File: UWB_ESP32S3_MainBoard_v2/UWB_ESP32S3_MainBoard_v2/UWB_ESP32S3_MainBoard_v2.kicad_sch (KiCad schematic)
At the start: 7 parts, among them J1 ESP32_S3_2, J2 ESP32_S3_1, J3 BNO085, J4 DRV8833_L_OUT, J5 DRV8833_L_IN, J6 DRV8833_R_OUT, J7 DRV8833_R_IN

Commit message: PCB재설계
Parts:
- added C1, C3: 470uF_16V, symbol Device:C
- added C10, C2, C4, C6, C8, C9: 0.1uF_50V, symbol Device:C
- added C5: 100uF_16V, symbol Device:C
- added C7: 100uF_50V, symbol Device:C
- added D1: D_Schottky, symbol Device:D_Schottky
- added D2: VBAT_LED, symbol Device:LED
- added D3: 5V0_LED, symbol Device:LED
- added D4: VCC_LED, symbol Device:LED
- added F1: PTC_2A, symbol Device:Fuse
- added J10: MP1584EN_IN, symbol Connector_Generic:Conn_01x06
- added J11: MP1584EN_OUT, symbol Connector_Generic:Conn_01x06
- added J12: MINI360_IN, symbol Connector_Generic:Conn_01x04
- added J13: MINI360_OUT, symbol Connector_Generic:Conn_01x04
- added J14: VBAT, symbol Connector:Screw_Terminal_01x02
- added J8: TAU_1201, symbol Connector_Generic:Conn_01x07
- added J9: ESP32_UWBAOA_UART, symbol Connector_Generic:Conn_01x02
- added R1: 4.7K, symbol Device:R
- added R2: 2.2K, symbol Device:R
- added R3: 1K, symbol Device:R
- added TP1: VBAT_SK, symbol Connector:TestPoint
- added TP2: 5V0, symbol Connector:TestPoint
- added TP3: 3V3_SENSOR, symbol Connector:TestPoint
- added TP4: GND, symbol Connector:TestPoint
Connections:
- net IO15 is gone; now on net L_IN4: J1.8 (Pin_8)
- net IO16 is gone; now on net L_IN3: J1.9 (Pin_9)
- net IO17 is gone; now on net L_IN2: J1.10 (Pin_10)
- net IO18 is gone; now on net L_IN1: J1.11 (Pin_11)
- net 3V3: now also J3.1 (Pin_1), J13.4 (Pin_4), J8.1 (Pin_1); no longer J1.1 (Pin_1), J1.2 (Pin_2)
- net 5V0: now also J11.6 (Pin_6), R2.1
- net GND: now also D2.1 (K), D3.1 (K), D4.1 (K), J10.1 (Pin_1), J11.1 (Pin_1), J12.1 (Pin_1), J13.1 (Pin_1), J14.2 (Pin_2), J8.2 (Pin_2)
- net L_IN1: no longer J1.7 (Pin_7)
- net L_IN2: no longer J1.6 (Pin_6)
- net L_IN3: no longer J1.5 (Pin_5)
- net L_IN4: no longer J1.4 (Pin_4)
- net VBAT_F: now also D1.2 (A), F1.2; no longer J4.4 (Pin_4), J7.4 (Pin_4)
- net VCC: now also R3.1; no longer J3.1 (Pin_1)
- new net: D3.2 (A), R2.2
- new net: D4.2 (A), R3.2
- new net: D2.2 (A), R1.2
- new net 3V3_ESP1: J1.1 (Pin_1)
- new net 3V3_ESP2: J1.2 (Pin_2)
- new net AOA_RX: J1.6 (Pin_6), J9.1 (Pin_1)
- new net AOA_TX: J1.7 (Pin_7), J9.2 (Pin_2)
- new net GNSS_R1: J1.4 (Pin_4), J8.4 (Pin_4)
- new net GNSS_T1: J1.5 (Pin_5), J8.3 (Pin_3)
- new net P: J8.7 (Pin_7)
- new net R2: J8.5 (Pin_5)
- new net T2: J8.6 (Pin_6)
- new net VBAT: F1.1, J14.1 (Pin_1)
- new net VBAT_SK: D1.1 (K), J10.6 (Pin_6), J12.4 (Pin_4), J4.4 (Pin_4), J7.4 (Pin_4), R1.1
- no-connect marks 21 -> 36
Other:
- note added: "3.3V RAIL"
- note added: "5V RAIL"
- note added: "ESP32, UWB"
- note added: "MODULE"
- note added: "VBAT_SK"
- moved on the sheet: J1, J2, J3, J4, J5, J6, J7

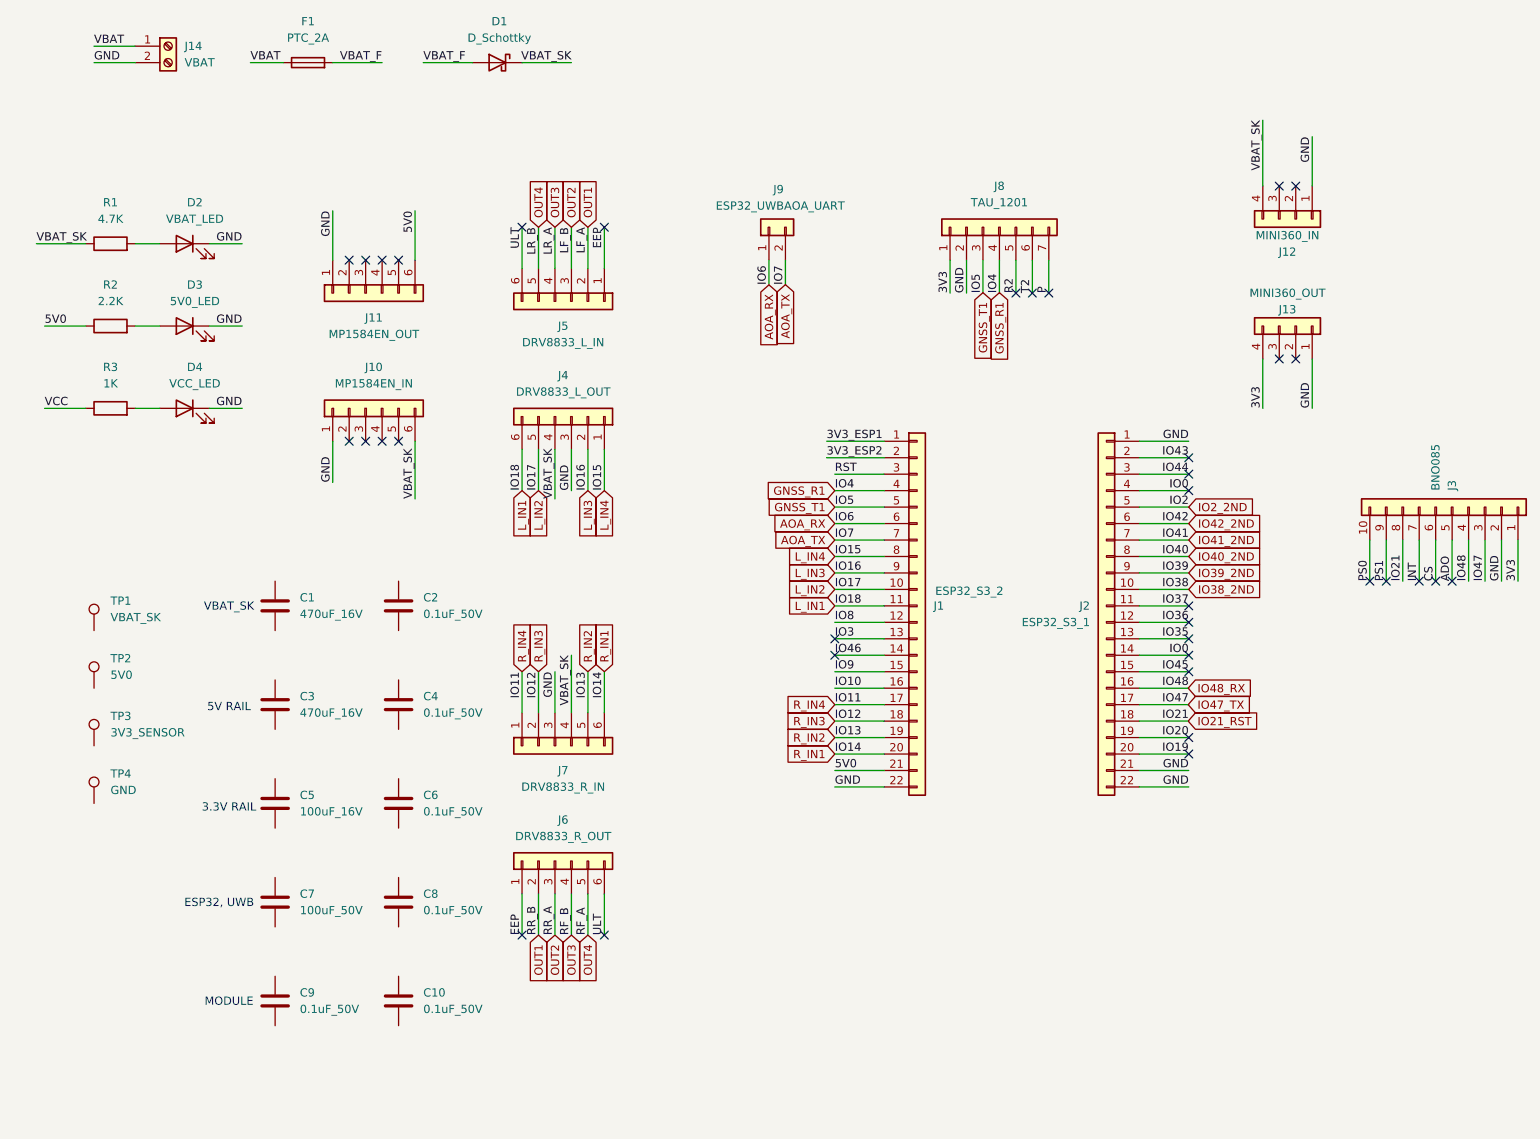
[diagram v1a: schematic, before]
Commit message: esp32-s3 기반 pcb 배치 시작
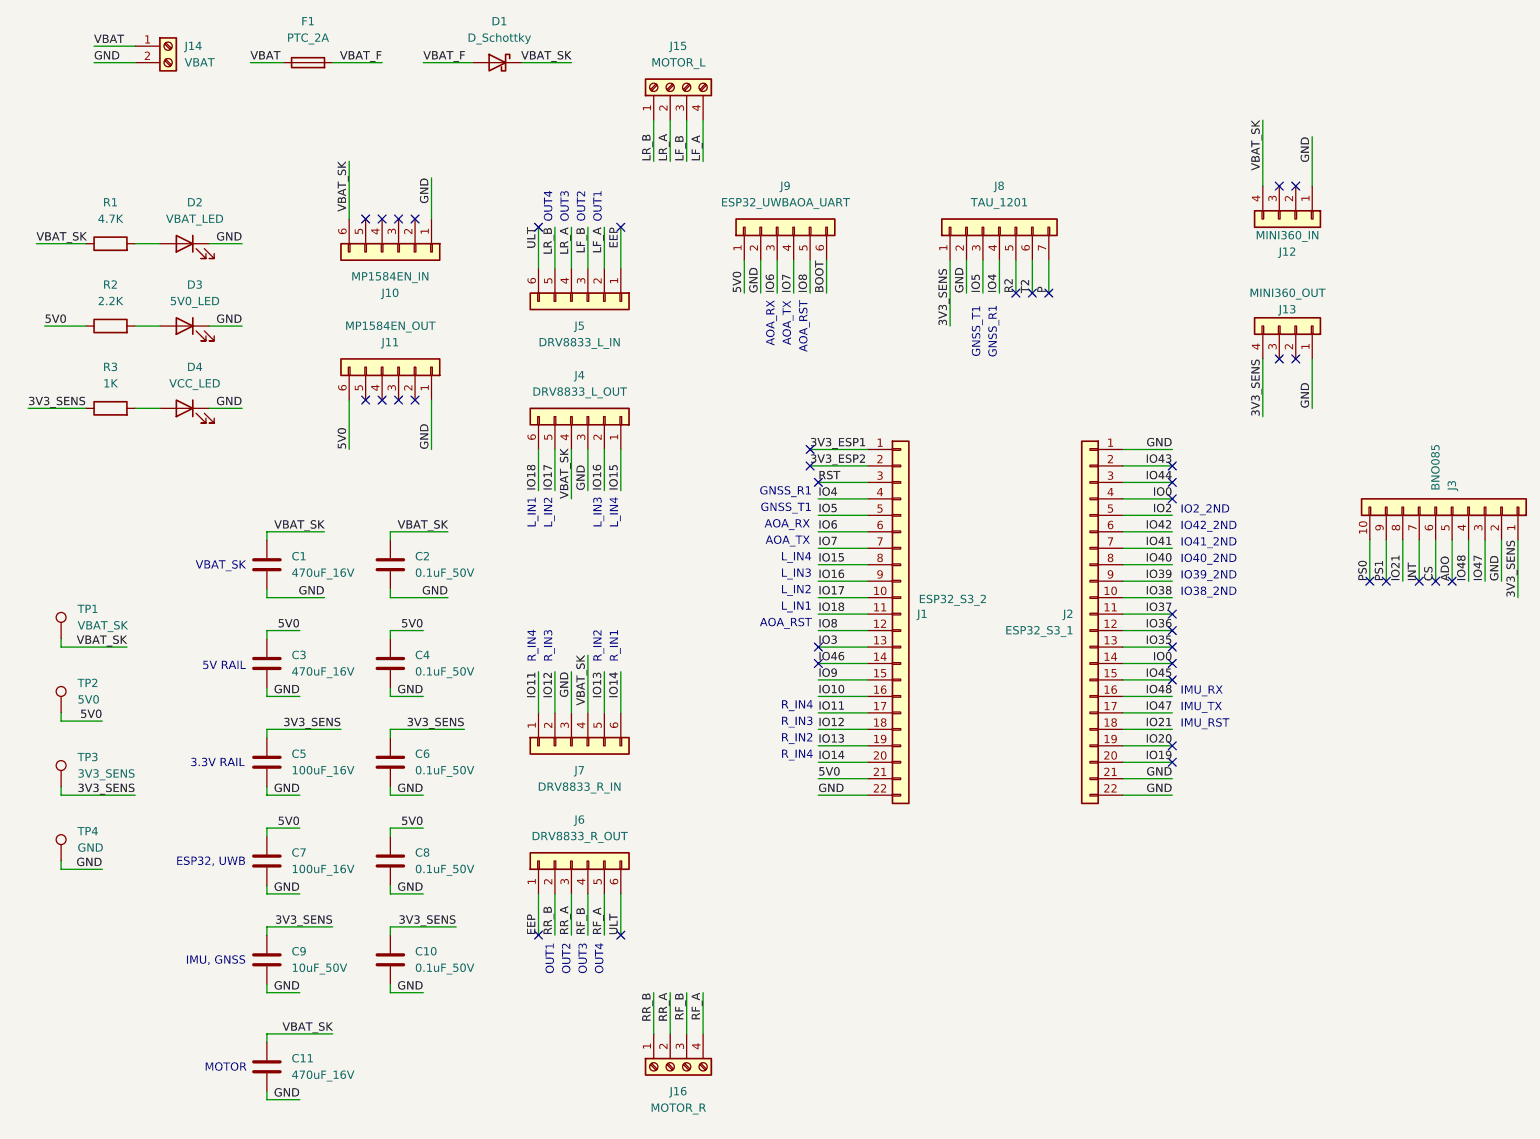
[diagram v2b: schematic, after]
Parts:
- removed J9: ESP32_UWBAOA_UART, symbol Connector_Generic:Conn_01x02
- added C11: 470uF_16V, Capacitor_THT:CP_Radial_D8.0mm_P3.50mm, symbol Device:C
- added J15: MOTOR_L, 10000_custom_Library:KF301_4P_5.00mm, symbol Connector:Screw_Terminal_01x04
- added J16: MOTOR_R, 10000_custom_Library:KF301_4P_5.00mm, symbol Connector:Screw_Terminal_01x04
- added J9: ESP32_UWBAOA_UART, Connector_JST:JST_XH_B6B-XH-A_1x06_P2.50mm_Vertical, symbol Connector_Generic:Conn_01x06
- C1, C3: footprint (none) -> Capacitor_THT:CP_Radial_D8.0mm_P3.50mm
- C10, C2, C4, C6, C8: footprint (none) -> Capacitor_SMD:C_0805_2012Metric_Pad1.18x1.45mm_HandSolder
- C5: footprint (none) -> Capacitor_THT:CP_Radial_D5.0mm_P2.00mm
- C7: value 100uF_50V -> 100uF_16V; footprint (none) -> Capacitor_THT:CP_Radial_D5.0mm_P2.00mm
- C9: value 0.1uF_50V -> 10uF_50V; footprint (none) -> Capacitor_SMD:C_0805_2012Metric_Pad1.18x1.45mm_HandSolder
- D1: footprint (none) -> Diode_SMD:D_SMA_Handsoldering
- D2, D3, D4: footprint (none) -> LED_SMD:LED_0805_2012Metric_Pad1.15x1.40mm_HandSolder
- F1: footprint (none) -> 10000_custom_Library:PTC_Radial_Disc_P5.08mm_Drill1.0mm
- J1, J2: footprint (none) -> Connector_PinSocket_2.54mm:PinSocket_1x22_P2.54mm_Vertical
- J10, J11, J4, J5, J6, J7: footprint (none) -> Connector_PinSocket_2.54mm:PinSocket_1x06_P2.54mm_Vertical
- J12, J13: footprint (none) -> Connector_PinSocket_2.54mm:PinSocket_1x04_P2.54mm_Vertical
- J14: footprint (none) -> 10000_custom_Library:KF301_2P_5.00mm
- J3: footprint (none) -> Connector_PinSocket_2.54mm:PinSocket_1x10_P2.54mm_Vertical
- J8: footprint (none) -> Connector_PinSocket_2.54mm:PinSocket_1x07_P2.54mm_Vertical
- R1, R2, R3: footprint (none) -> Resistor_SMD:R_0805_2012Metric_Pad1.20x1.40mm_HandSolder
- TP1, TP2, TP4: footprint (none) -> TestPoint:TestPoint_Pad_D2.0mm
- TP3: value 3V3_SENSOR -> 3V3_SENS; footprint (none) -> TestPoint:TestPoint_Pad_D2.0mm
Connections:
- net 3V3 is gone; now on net 3V3_SENS: J13.4 (Pin_4), J3.1 (Pin_1), J8.1 (Pin_1)
- net VCC is gone; now on net 3V3_SENS: R3.1
- net 5V0: now also C3.1, C4.1, C7.1, C8.1, TP2.1, J9.1 (Pin_1)
- net GND: now also C1.2, C10.2, C2.2, C3.2, C4.2, C5.2, C6.2, C7.2, C8.2, C9.2, TP4.1, C11.2, J9.2 (Pin_2)
- net IO8: now also J9.5 (Pin_5)
- net VBAT_SK: now also C1.1, C2.1, TP1.1, C11.1
- net 3V3_SENS: now reaches TP3.1
- net 3V3_SENS: now also C10.1, C5.1, C6.1, C9.1
- net AOA_RX renamed IO6
- net IO6: now also J9.3 (Pin_3)
- net AOA_TX renamed IO7
- net IO7: now also J9.4 (Pin_4)
- net GNSS_R1 renamed IO4
- net GNSS_T1 renamed IO5
- net IO21_RST renamed IO21
- net IO2_2ND renamed IO2
- net IO38_2ND renamed IO38
- net IO39_2ND renamed IO39
- net IO40_2ND renamed IO40
- net IO41_2ND renamed IO41
- net IO42_2ND renamed IO42
- net IO47_TX renamed IO47
- net IO48_RX renamed IO48
- net L_IN1 renamed IO18
- net L_IN2 renamed IO17
- net L_IN3 renamed IO16
- net L_IN4 renamed IO15
- net OUT1 renamed LF_A
- net LF_A: now also J15.4 (Pin_4); no longer J6.2 (Pin_2)
- net OUT2 renamed LF_B
- net LF_B: now also J15.3 (Pin_3); no longer J6.3 (Pin_3)
- net OUT3 renamed LR_A
- net LR_A: now also J15.2 (Pin_2); no longer J6.4 (Pin_4)
- net OUT4 renamed LR_B
- net LR_B: now also J15.1 (Pin_1); no longer J6.5 (Pin_5)
- net R_IN1 renamed IO14
- net R_IN2 renamed IO13
- net R_IN3 renamed IO12
- net R_IN4 renamed IO11
- new net BOOT: J9.6 (Pin_6)
- new net RF_A: J16.4 (Pin_4), J6.5 (Pin_5)
- new net RF_B: J16.3 (Pin_3), J6.4 (Pin_4)
- new net RR_A: J16.2 (Pin_2), J6.3 (Pin_3)
- new net RR_B: J16.1 (Pin_1), J6.2 (Pin_2)
- no-connect marks 36 -> 39
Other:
- note added: "AOA_RST"
- note added: "AOA_RX"
- note added: "AOA_TX"
- note added: "GNSS_R1"
- note added: "GNSS_T1"
- note added: "IMU, GNSS"
- note added: "IMU_RST"
- note added: "IMU_RX"
- note added: "IMU_TX"
- note added: "IO2_2ND"
- note added: "IO38_2ND"
- note added: "IO39_2ND"
- note added: "IO40_2ND"
- note added: "IO41_2ND"
- note added: "IO42_2ND"
- note added: "L_IN1"
- note added: "L_IN2"
- note added: "L_IN3"
- note added: "L_IN4"
- note added: "MOTOR"
- note added: "OUT1"
- note added: "OUT2"
- note added: "OUT3"
- note added: "OUT4"
- note added: "R_IN1"
- note added: "R_IN2"
- note added: "R_IN3"
- note added: "R_IN4"
- note removed: "MODULE"
- moved on the sheet: C1, C10, C2, C3, C4, C5, C6, C7, C8, C9, J1, J10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

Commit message: 배치 완료, 풋프린트 추가 등
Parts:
- added C12: 10uF_50V, Capacitor_SMD:C_0805_2012Metric_Pad1.18x1.45mm_HandSolder, symbol Device:C
- added C13: 0.1uF_50V, Capacitor_SMD:C_0805_2012Metric_Pad1.18x1.45mm_HandSolder, symbol Device:C
- added C14: 100uF_16V, Capacitor_THT:CP_Radial_D5.0mm_P2.00mm, symbol Device:C
- C11: value 470uF_16V -> 100uF_16V; footprint Capacitor_THT:CP_Radial_D8.0mm_P3.50mm -> Capacitor_THT:CP_Radial_D5.0mm_P2.00mm
- renumbered D2 to D1, D3 to D2, D4 to D3, D1 to D4
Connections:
- net 3V3_SENS: now also C12.1, C13.1
- net GND: now also C12.2, C13.2, C14.2
- net IO0: no longer J2.4 (Pin_4)
- net VBAT_SK: now also C14.1
- new net IO1: J2.4 (Pin_4)
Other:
- note added: "GNSS"
- note added: "IMU"
- note added: "MOTOR_L"
- note added: "MOTOR_R"
- note removed: "IMU, GNSS"
- note removed: "MOTOR"
- moved on the sheet: C11
